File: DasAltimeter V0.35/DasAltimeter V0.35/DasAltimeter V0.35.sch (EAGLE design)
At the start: 56 parts, among them IC1 BMI055, U1 ATSAMD21G-A, U2 3.3V/150mA, U3 MS5803-14BA, U5 ADXL377, X1 22-23-2041, X2 22-23-2041

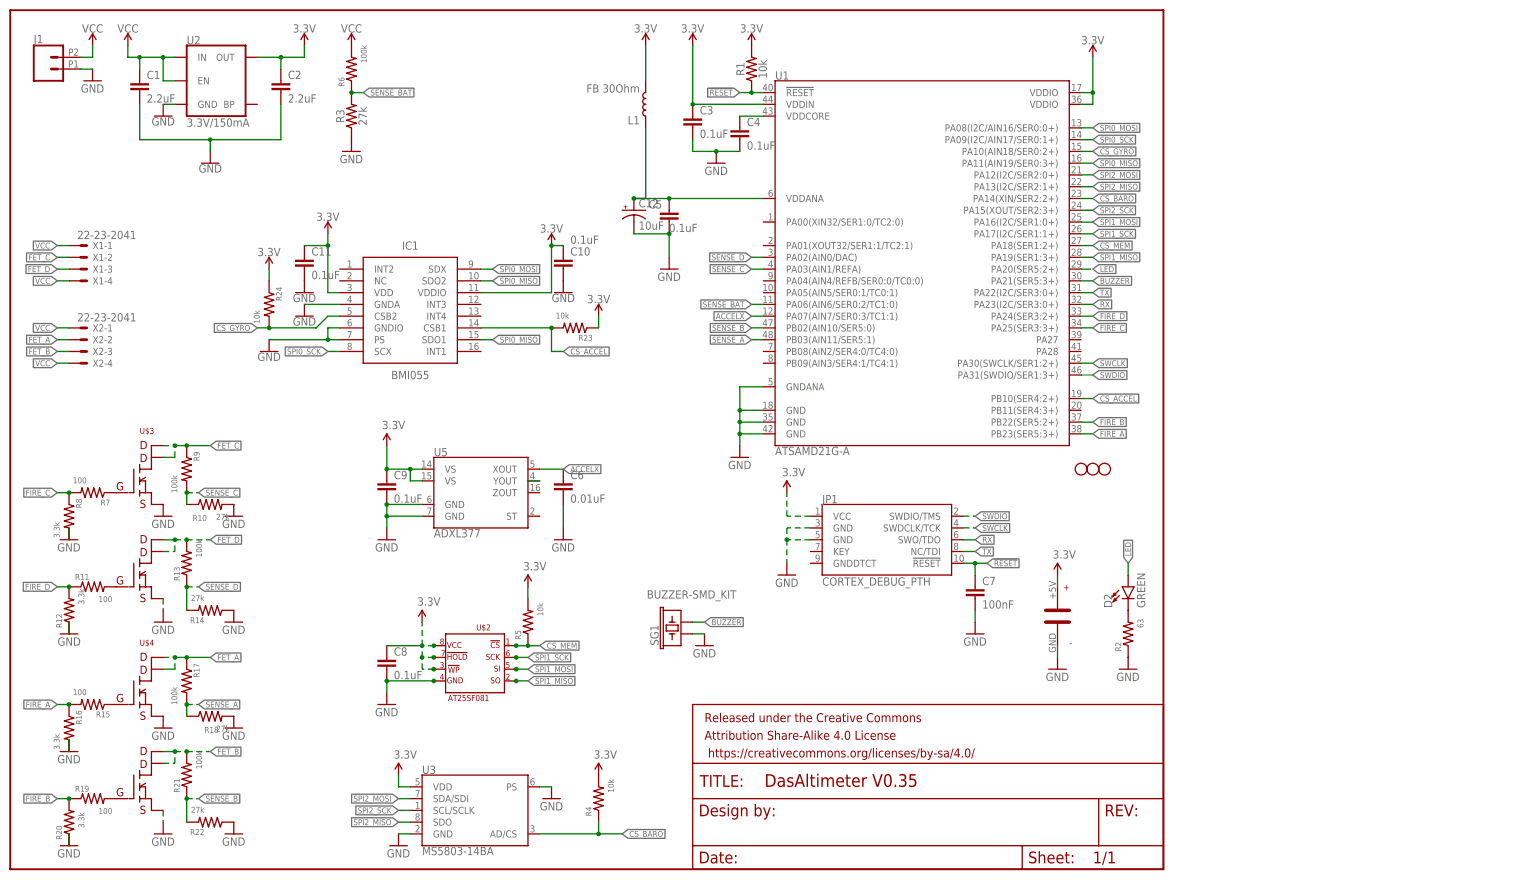
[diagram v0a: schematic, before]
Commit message: routed dasAltimeter V0.40 and updates to code
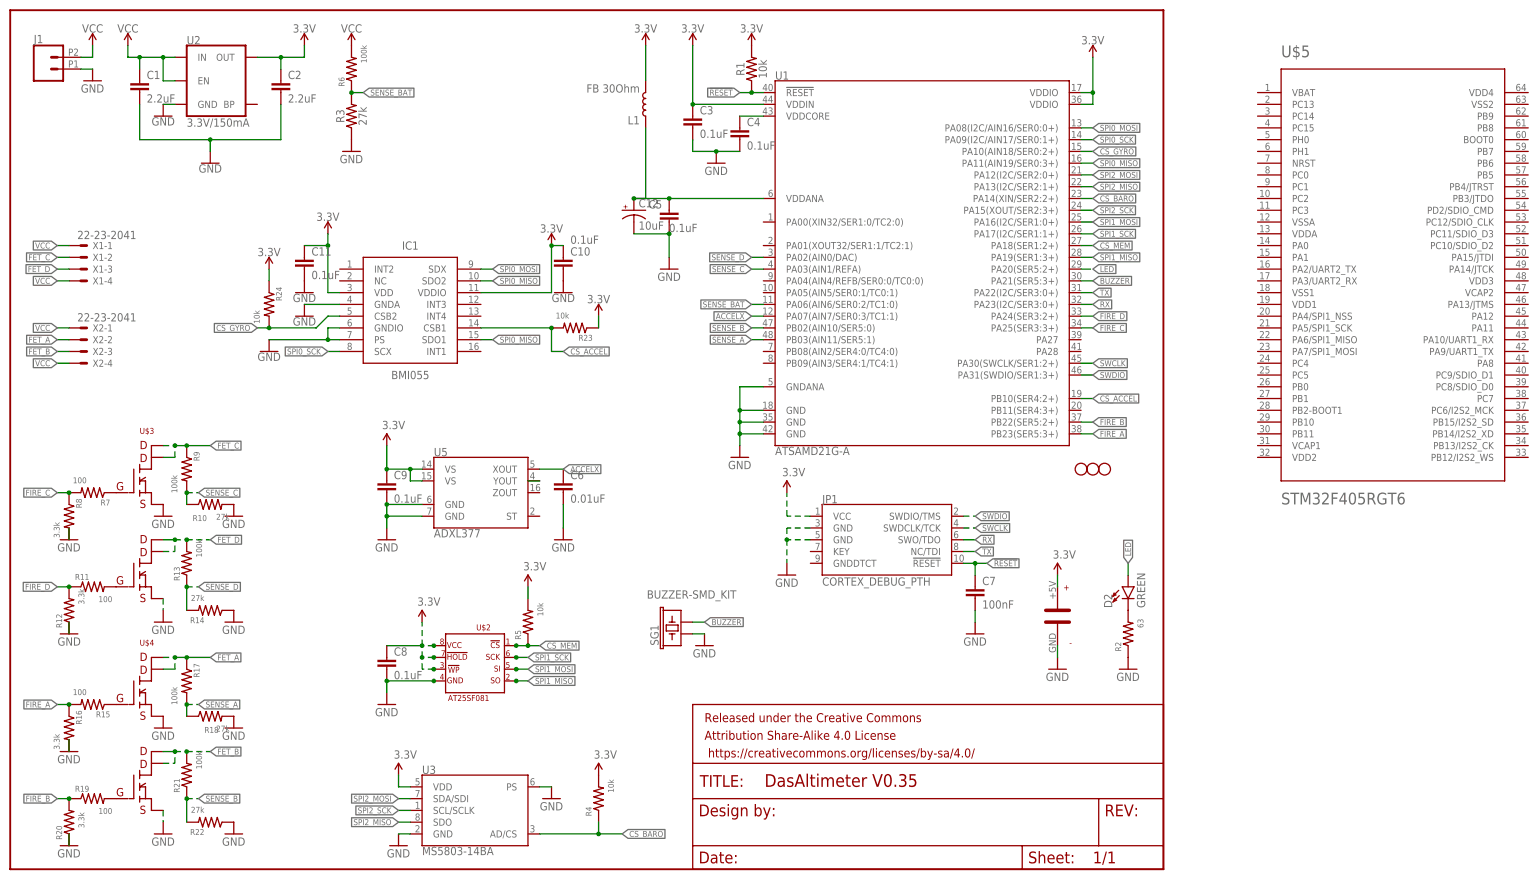
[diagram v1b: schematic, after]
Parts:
- added U$5: STM32F405RGT6, SparkFun-IC-Microcontroller:STM32F405RG
